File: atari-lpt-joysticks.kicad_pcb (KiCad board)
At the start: 2 copper layers, 55.9 x 30.5 mm, 5 parts, among them J1 DB25_Male, J2 Barrel_Jack_Switch

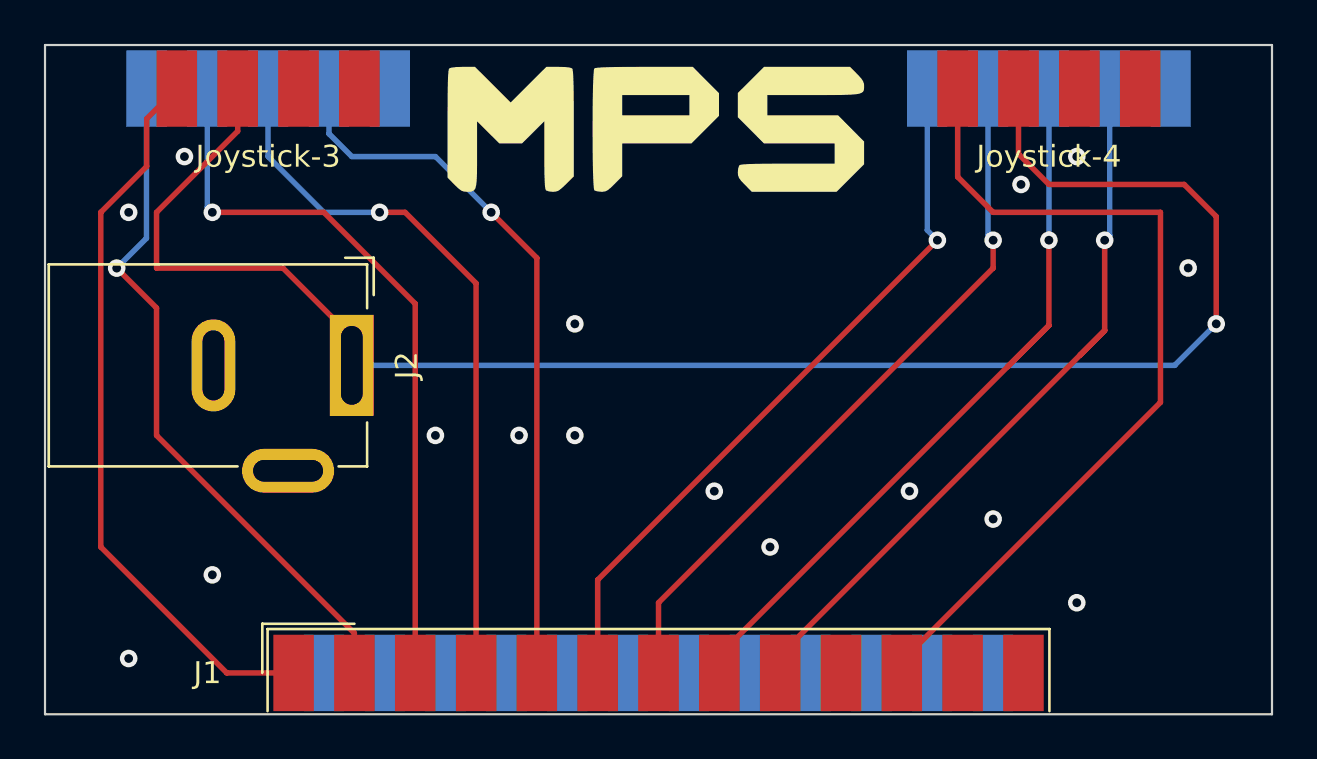
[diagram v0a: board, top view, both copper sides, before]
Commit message: swap joystick 3 and 4
hardware description are not correct :
 * http://atari4ever.free.fr/hardware/zip/4joy_ada.zip
 * https://www.atari-forum.com/viewtopic.php?p=318615#p318615

Gauntlet 2 and Leatherneck game use this pinout

Discussion : https://github.com/hatari/hatari/pull/22
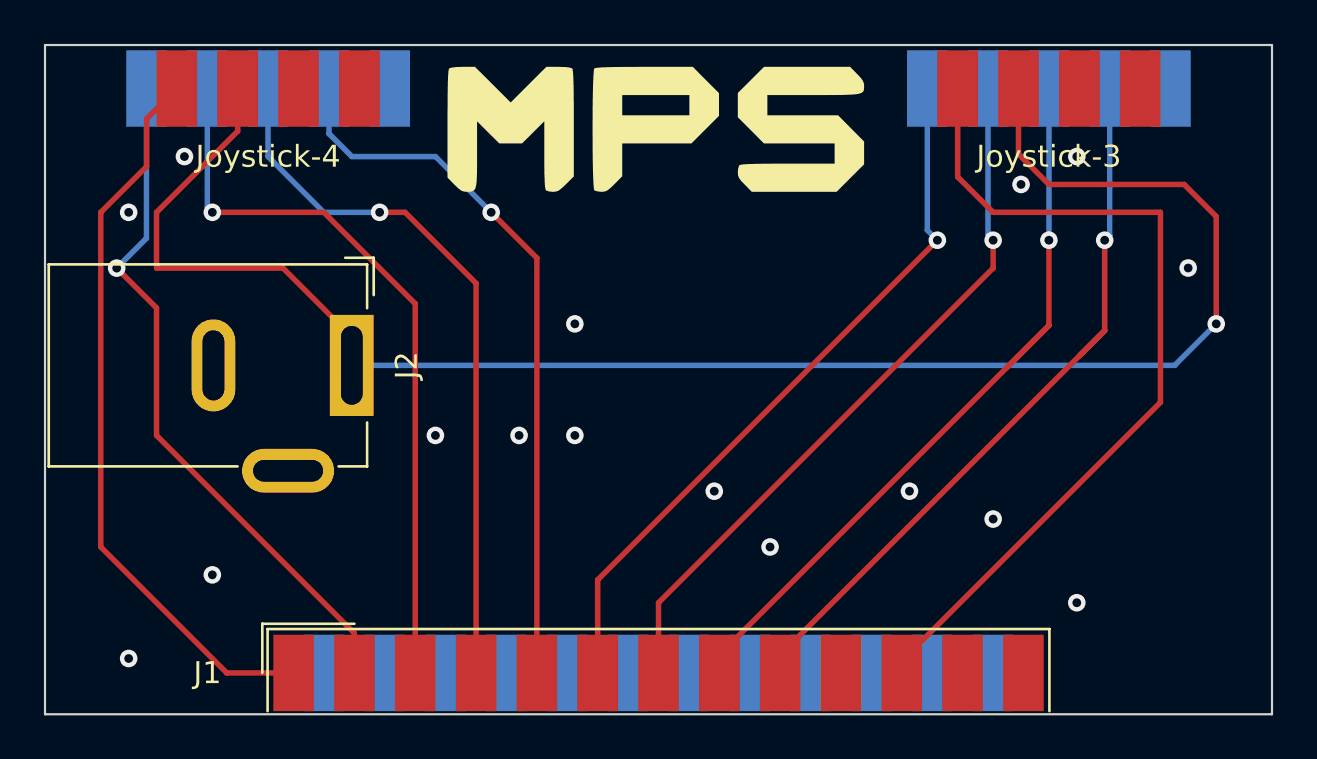
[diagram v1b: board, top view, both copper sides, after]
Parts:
- renumbered Joystick-4 to Joystick-3, Joystick-3 to Joystick-4
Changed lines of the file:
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@@
   )
   (net 0 "")
-  (net 1 "Net-(Joystick-3-Pad6)")
-  (net 2 "Net-(Joystick-3-Pad1)")
-  (net 3 "Net-(Joystick-3-Pad2)")
-  (net 4 "Net-(Joystick-3-Pad3)")
-  (net 5 "Net-(Joystick-3-Pad4)")
-  (net 6 "Net-(Joystick-4-Pad1)")
-  (net 7 "Net-(Joystick-4-Pad2)")
-  (net 8 "Net-(Joystick-4-Pad3)")
-  (net 9 "Net-(Joystick-4-Pad4)")
+  (net 1 "Net-(J1-Pad1)")
+  (net 2 "Net-(J1-Pad2)")
+  (net 3 "Net-(J1-Pad3)")
+  (net 4 "Net-(J1-Pad4)")
+  (net 5 "Net-(J1-Pad5)")
+  (net 6 "Net-(J1-Pad6)")
+  (net 7 "Net-(J1-Pad7)")
+  (net 8 "Net-(J1-Pad8)")
+  (net 9 "Net-(J1-Pad9)")
   (net 10 "unconnected-(J1-Pad10)")
-  (net 11 "Net-(Joystick-4-Pad6)")
+  (net 11 "Net-(J1-Pad11)")
   (net 12 "unconnected-(J1-Pad12)")
   (net 13 "unconnected-(J1-Pad13)")
@@
   (net 16 "unconnected-(J1-Pad16)")
   (net 17 "unconnected-(J1-Pad17)")
-  (net 18 "Net-(Joystick-3-Pad7)")
+  (net 18 "Net-(J2-Pad1)")
   (net 19 "unconnected-(Joystick-3-Pad5)")
   (net 20 "unconnected-(Joystick-3-Pad9)")
@@
     (fp_line (start 2.17 1.99) (end 3.37 1.99) (layer "F.Fab") (width 0.1))
     (pad "1" smd rect (at -16.62 0) (size 1.846667 3.48) (layers "F.Cu" "F.Paste" "F.Mask")
-      (net 1 "Net-(Joystick-3-Pad6)") (pinfunction "1") (pintype "passive"))
+      (net 1 "Net-(J1-Pad1)") (pinfunction "1") (pintype "passive"))
     (pad "2" smd rect (at -13.85 0) (size 1.846667 3.48) (layers "F.Cu" "F.Paste" "F.Mask")
-      (net 2 "Net-(Joystick-3-Pad1)") (pinfunction "2") (pintype "passive"))
+      (net 2 "Net-(J1-Pad2)") (pinfunction "2") (pintype "passive"))
     (pad "3" smd rect (at -11.08 0) (size 1.846667 3.48) (layers "F.Cu" "F.Paste" "F.Mask")
-      (net 3 "Net-(Joystick-3-Pad2)") (pinfunction "3") (pintype "passive"))
+      (net 3 "Net-(J1-Pad3)") (pinfunction "3") (pintype "passive"))
     (pad "4" smd rect (at -8.31 0) (size 1.846667 3.48) (layers "F.Cu" "F.Paste" "F.Mask")
-      (net 4 "Net-(Joystick-3-Pad3)") (pinfunction "4") (pintype "passive"))
+      (net 4 "Net-(J1-Pad4)") (pinfunction "4") (pintype "passive"))
     (pad "5" smd rect (at -5.54 0) (size 1.846667 3.48) (layers "F.Cu" "F.Paste" "F.Mask")
-      (net 5 "Net-(Joystick-3-Pad4)") (pinfunction "5") (pintype "passive"))
+      (net 5 "Net-(J1-Pad5)") (pinfunction "5") (pintype "passive"))
     (pad "6" smd rect (at -2.77 0) (size 1.846667 3.48) (layers "F.Cu" "F.Paste" "F.Mask")
-      (net 6 "Net-(Joystick-4-Pad1)") (pinfunction "6") (pintype "passive"))
+      (net 6 "Net-(J1-Pad6)") (pinfunction "6") (pintype "passive"))
     (pad "7" smd rect (at 0 0) (size 1.846667 3.48) (layers "F.Cu" "F.Paste" "F.Mask")
-      (net 7 "Net-(Joystick-4-Pad2)") (pinfunction "7") (pintype "passive"))
+      (net 7 "Net-(J1-Pad7)") (pinfunction "7") (pintype "passive"))
     (pad "8" smd rect (at 2.77 0) (size 1.846667 3.48) (layers "F.Cu" "F.Paste" "F.Mask")
-      (net 8 "Net-(Joystick-4-Pad3)") (pinfunction "8") (pintype "passive"))
+      (net 8 "Net-(J1-Pad8)") (pinfunction "8") (pintype "passive"))
     (pad "9" smd rect (at 5.54 0) (size 1.846667 3.48) (layers "F.Cu" "F.Paste" "F.Mask")
-      (net 9 "Net-(Joystick-4-Pad4)") (pinfunction "9") (pintype "passive"))
+      (net 9 "Net-(J1-Pad9)") (pinfunction "9") (pintype "passive"))
     (pad "10" smd rect (at 8.31 0) (size 1.846667 3.48) (layers "F.Cu" "F.Paste" "F.Mask")
       (net 10 "unconnected-(J1-Pad10)") (pinfunction "10") (pintype "passive+no_connect"))
     (pad "11" smd rect (at 11.08 0) (size 1.846667 3.48) (layers "F.Cu" "F.Paste" "F.Mask")
-      (net 11 "Net-(Joystick-4-Pad6)") (pinfunction "11") (pintype "passive"))
+      (net 11 "Net-(J1-Pad11)") (pinfunction "11") (pintype "passive"))
     (pad "12" smd rect (at 13.85 0) (size 1.846667 3.48) (layers "F.Cu" "F.Paste" "F.Mask")
       (net 12 "unconnected-(J1-Pad12)") (pinfunction "12") (pintype "passive+no_connect"))
@@
     (fp_line (start -4.5 13.7) (end -4.5 0.4) (layer "F.Fab") (width 0.1))
     (pad "1" thru_hole rect (at 0 0 270) (size 4.6 2) (drill oval 3.6 1) (layers *.Cu *.Mask)
-      (net 18 "Net-(Joystick-3-Pad7)") (pintype "passive"))
+      (net 18 "Net-(J2-Pad1)") (pintype "passive"))
     (pad "2" thru_hole oval (at 0 6.3 270) (size 4.2 2) (drill oval 3.2 1) (layers *.Cu *.Mask)
       (net 23 "GND") (pintype "passive"))
@@
     (property "Sheetname" "")
     (attr smd)
-    (fp_text reference "Joystick-3" (at 0 3.0975) (layer "F.SilkS")
+    (fp_text reference "Joystick-4" (at 0 3.0975) (layer "F.SilkS")
       (effects (font (size 1 1) (thickness 0.15)))
     )
@@
     (fp_line (start 1.985 -1.99) (end 1.985 0.91) (layer "F.Fab") (width 0.1))
     (pad "1" smd rect (at -5.54 0) (size 1.846667 3.48) (layers "B.Cu" "B.Paste" "B.Mask")
-      (net 2 "Net-(Joystick-3-Pad1)") (pinfunction "1") (pintype "passive"))
+      (net 2 "Net-(J1-Pad2)") (pinfunction "1") (pintype "passive"))
     (pad "2" smd rect (at -2.77 0) (size 1.846667 3.48) (layers "B.Cu" "B.Paste" "B.Mask")
-      (net 3 "Net-(Joystick-3-Pad2)") (pinfunction "2") (pintype "passive"))
+      (net 3 "Net-(J1-Pad3)") (pinfunction "2") (pintype "passive"))
     (pad "3" smd rect (at 0 0) (size 1.846667 3.48) (layers "B.Cu" "B.Paste" "B.Mask")
-      (net 4 "Net-(Joystick-3-Pad3)") (pinfunction "3") (pintype "passive"))
+      (net 4 "Net-(J1-Pad4)") (pinfunction "3") (pintype "passive"))
     (pad "4" smd rect (at 2.77 0) (size 1.846667 3.48) (layers "B.Cu" "B.Paste" "B.Mask")
-      (net 5 "Net-(Joystick-3-Pad4)") (pinfunction "4") (pintype "passive"))
+      (net 5 "Net-(J1-Pad5)") (pinfunction "4") (pintype "passive"))
     (pad "5" smd rect (at 5.54 0) (size 1.846667 3.48) (layers "B.Cu" "B.Paste" "B.Mask")
-      (net 19 "unconnected-(Joystick-3-Pad5)") (pinfunction "5") (pintype "passive+no_connect"))
+      (net 21 "unconnected-(Joystick-4-Pad5)") (pinfunction "5") (pintype "passive+no_connect"))
     (pad "6" smd rect (at -4.155 0) (size 1.846667 3.48) (layers "F.Cu" "F.Paste" "F.Mask")
-      (net 1 "Net-(Joystick-3-Pad6)") (pinfunction "6") (pintype "passive"))
+      (net 1 "Net-(J1-Pad1)") (pinfunction "6") (pintype "passive"))
     (pad "7" smd rect (at -1.385 0) (size 1.846667 3.48) (layers "F.Cu" "F.Paste" "F.Mask")
-      (net 18 "Net-(Joystick-3-Pad7)") (pinfunction "7") (pintype "passive"))
+      (net 18 "Net-(J2-Pad1)") (pinfunction "7") (pintype "passive"))
     (pad "8" smd rect (at 1.385 0) (size 1.846667 3.48) (layers "F.Cu" "F.Paste" "F.Mask")
       (net 23 "GND") (pinfunction "8") (pintype "passive"))
     (pad "9" smd rect (at 4.155 0) (size 1.846667 3.48) (layers "F.Cu" "F.Paste" "F.Mask")
-      (net 20 "unconnected-(Joystick-3-Pad9)") (pinfunction "9") (pintype "passive+no_connect"))
+      (net 22 "unconnected-(Joystick-4-Pad9)") (pinfunction "9") (pintype "passive+no_connect"))
     (model "${KICAD6_3DMODEL_DIR}/Connector_Dsub.3dshapes/DSUB-9_Male_EdgeMount_P2.77mm.wrl"
       (offset (xyz 0 0 0))
@@
     (property "Sheetname" "")
     (attr smd)
-    (fp_text reference "Joystick-4" (at 0 3.0975) (layer "F.SilkS")
+    (fp_text reference "Joystick-3" (at 0 3.0975) (layer "F.SilkS")
       (effects (font (size 1 1) (thickness 0.15)))
     )
@@
     (fp_line (start -3.555 0.91) (end -4.755 0.91) (layer "F.Fab") (width 0.1))
     (pad "1" smd rect (at -5.54 0) (size 1.846667 3.48) (layers "B.Cu" "B.Paste" "B.Mask")
-      (net 6 "Net-(Joystick-4-Pad1)") (pinfunction "1") (pintype "passive"))
+      (net 6 "Net-(J1-Pad6)") (pinfunction "1") (pintype "passive"))
     (pad "2" smd rect (at -2.77 0) (size 1.846667 3.48) (layers "B.Cu" "B.Paste" "B.Mask")
-      (net 7 "Net-(Joystick-4-Pad2)") (pinfunction "2") (pintype "passive"))
+      (net 7 "Net-(J1-Pad7)") (pinfunction "2") (pintype "passive"))
     (pad "3" smd rect (at 0 0) (size 1.846667 3.48) (layers "B.Cu" "B.Paste" "B.Mask")
-      (net 8 "Net-(Joystick-4-Pad3)") (pinfunction "3") (pintype "passive"))
+      (net 8 "Net-(J1-Pad8)") (pinfunction "3") (pintype "passive"))
     (pad "4" smd rect (at 2.77 0) (size 1.846667 3.48) (layers "B.Cu" "B.Paste" "B.Mask")
-      (net 9 "Net-(Joystick-4-Pad4)") (pinfunction "4") (pintype "passive"))
+      (net 9 "Net-(J1-Pad9)") (pinfunction "4") (pintype "passive"))
     (pad "5" smd rect (at 5.54 0) (size 1.846667 3.48) (layers "B.Cu" "B.Paste" "B.Mask")
-      (net 21 "unconnected-(Joystick-4-Pad5)") (pinfunction "5") (pintype "passive+no_connect"))
+      (net 19 "unconnected-(Joystick-3-Pad5)") (pinfunction "5") (pintype "passive+no_connect"))
     (pad "6" smd rect (at -4.155 0) (size 1.846667 3.48) (layers "F.Cu" "F.Paste" "F.Mask")
-      (net 11 "Net-(Joystick-4-Pad6)") (pinfunction "6") (pintype "passive"))
+      (net 11 "Net-(J1-Pad11)") (pinfunction "6") (pintype "passive"))
     (pad "7" smd rect (at -1.385 0) (size 1.846667 3.48) (layers "F.Cu" "F.Paste" "F.Mask")
-      (net 18 "Net-(Joystick-3-Pad7)") (pinfunction "7") (pintype "passive"))
+      (net 18 "Net-(J2-Pad1)") (pinfunction "7") (pintype "passive"))
     (pad "8" smd rect (at 1.385 0) (size 1.846667 3.48) (layers "F.Cu" "F.Paste" "F.Mask")
       (net 23 "GND") (pinfunction "8") (pintype "passive"))
     (pad "9" smd rect (at 4.155 0) (size 1.846667 3.48) (layers "F.Cu" "F.Paste" "F.Mask")
-      (net 22 "unconnected-(Joystick-4-Pad9)") (pinfunction "9") (pintype "passive+no_connect"))
+      (net 20 "unconnected-(Joystick-3-Pad9)") (pinfunction "9") (pintype "passive+no_connect"))
     (model "${KICAD6_3DMODEL_DIR}/Connector_Dsub.3dshapes/DSUB-9_Male_EdgeMount_P2.77mm.wrl"
       (offset (xyz 0 0 0))
